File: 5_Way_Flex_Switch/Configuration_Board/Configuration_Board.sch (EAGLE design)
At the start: 1 part

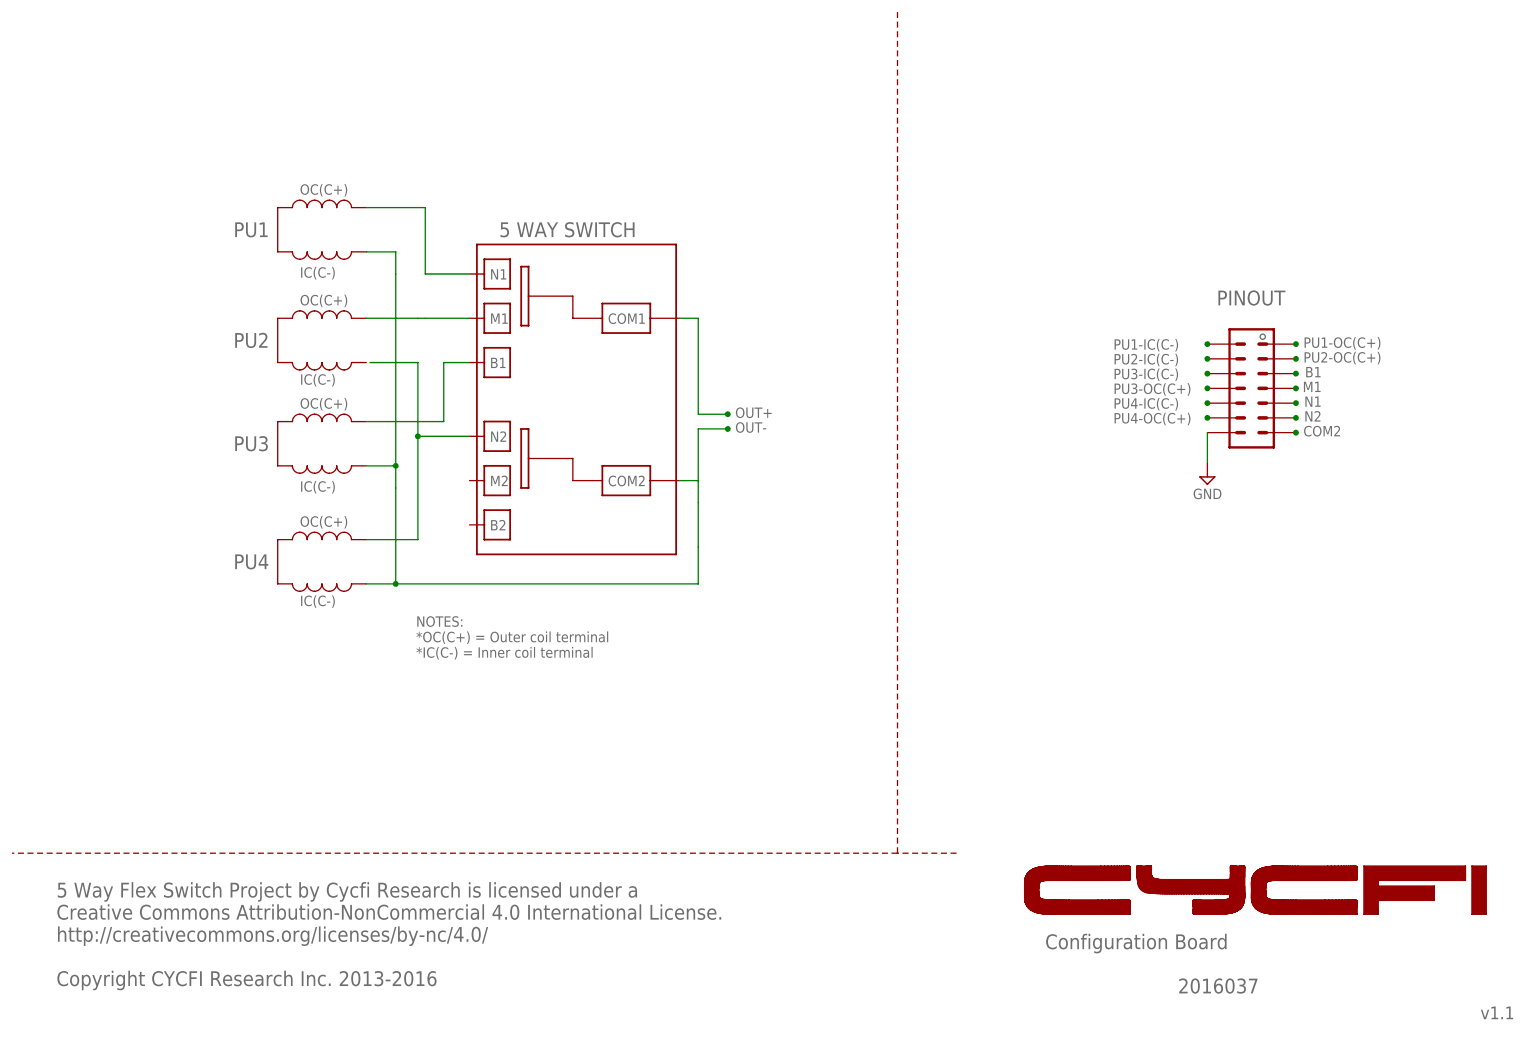
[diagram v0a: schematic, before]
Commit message: Updates/ label modifications to make them consistent
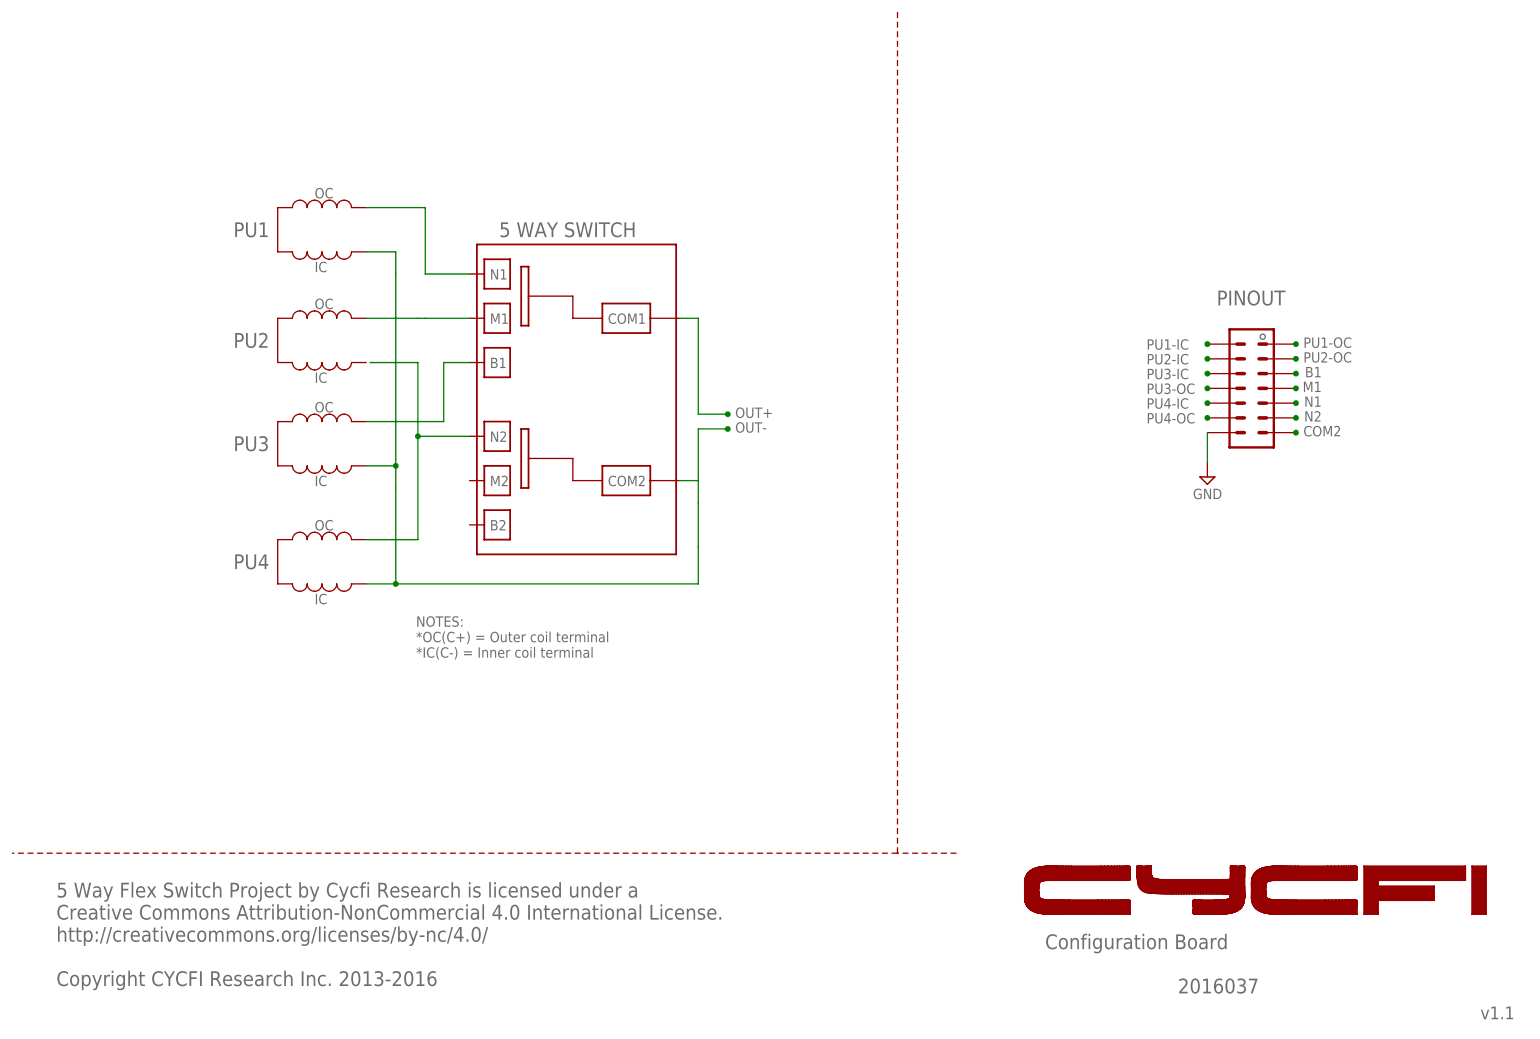
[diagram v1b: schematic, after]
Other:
- note added: "IC"
- note added: "OC"
- note added: "PU1-IC"
- note added: "PU1-OC"
- note added: "PU2-IC"
- note added: "PU2-OC"
- note added: "PU3-IC"
- note added: "PU3-OC"
- note added: "PU4-IC"
- note added: "PU4-OC"
- note removed: "IC(C-)"
- note removed: "OC(C+)"
- note removed: "PU1-IC(C-)"
- note removed: "PU1-OC(C+)"
- note removed: "PU2-IC(C-)"
- note removed: "PU2-OC(C+)"
- note removed: "PU3-IC(C-)"
- note removed: "PU3-OC(C+)"
- note removed: "PU4-IC(C-)"
- note removed: "PU4-OC(C+)"
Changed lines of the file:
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@@
 <setting verticaltext="up"/>
 </settings>
-<grid distance="0.1" unitdist="inch" unit="inch" style="lines" multiple="1" display="no" altdistance="0.01" altunitdist="inch" altunit="inch"/>
+<grid distance="0.1" unitdist="inch" unit="inch" style="lines" multiple="1" display="yes" altdistance="0.01" altunitdist="inch" altunit="inch"/>
 <layers>
 <layer number="1" name="Top" color="4" fill="1" visible="no" active="no"/>
@@
 <wire x1="58.42" y1="139.065" x2="60.96" y2="139.065" width="0.1524" layer="94"/>
 <wire x1="45.72" y1="146.685" x2="45.72" y2="139.065" width="0.1524" layer="94"/>
-<text x="49.53" y="134.62" size="1.778" layer="95">IC(C-)</text>
-<text x="49.53" y="148.9075" size="1.778" layer="95">OC(C+) </text>
 <wire x1="58.42" y1="127.635" x2="60.96" y2="127.635" width="0.1524" layer="94"/>
 <wire x1="58.42" y1="127.635" x2="57.15" y2="128.905" width="0.1524" layer="94" curve="90"/>
@@
 <vertex x="232.684540625" y="25.047221875"/>
 </polygon>
-<text x="49.53" y="129.8575" size="1.778" layer="95">OC(C+) </text>
-<text x="49.53" y="112.0775" size="1.778" layer="95">OC(C+) </text>
-<text x="49.53" y="91.7575" size="1.778" layer="95">OC(C+) </text>
-<text x="49.53" y="116.205" size="1.778" layer="95">IC(C-)</text>
-<text x="49.53" y="78.105" size="1.778" layer="95">IC(C-)</text>
-<text x="49.53" y="97.79" size="1.778" layer="95">IC(C-)</text>
 <text x="69.5325" y="69.215" size="1.778" layer="95">NOTES:
 *OC(C+) = Outer coil terminal
@@
 <text x="225.425" y="109.855" size="1.778" layer="95" rot="MR0">N2</text>
 <text x="207.3275" y="129.8575" size="2.54" layer="95">PINOUT</text>
-<text x="189.5475" y="122.2375" size="1.778" layer="95">PU1-IC(C-)</text>
-<text x="222.25" y="122.555" size="1.778" layer="95">PU1-OC(C+)</text>
-<text x="189.5475" y="119.6975" size="1.778" layer="95">PU2-IC(C-)</text>
-<text x="222.25" y="120.015" size="1.778" layer="95">PU2-OC(C+)</text>
-<text x="189.5475" y="117.1575" size="1.778" layer="95">PU3-IC(C-)</text>
-<text x="189.5475" y="114.6175" size="1.778" layer="95">PU3-OC(C+)</text>
-<text x="189.5475" y="112.0775" size="1.778" layer="95">PU4-IC(C-)</text>
-<text x="189.5475" y="109.5375" size="1.778" layer="95">PU4-OC(C+)</text>
+<text x="195.2625" y="122.2375" size="1.778" layer="95">PU1-IC</text>
+<text x="222.25" y="122.555" size="1.778" layer="95">PU1-OC</text>
+<text x="195.2625" y="119.6975" size="1.778" layer="95">PU2-IC</text>
+<text x="222.25" y="120.015" size="1.778" layer="95">PU2-OC</text>
+<text x="195.2625" y="117.1575" size="1.778" layer="95">PU3-IC</text>
+<text x="195.2625" y="114.6175" size="1.778" layer="95">PU3-OC</text>
+<text x="195.2625" y="112.0775" size="1.778" layer="95">PU4-IC</text>
+<text x="195.2625" y="109.5375" size="1.778" layer="95">PU4-OC</text>
 <text x="222.25" y="107.315" size="1.778" layer="95">COM2</text>
 <circle x="215.265" y="124.46" radius="0.4490125" width="0.1524" layer="95"/>
@@
 <wire x1="152.4" y1="35.56" x2="0" y2="35.56" width="0.1524" layer="94" style="longdash"/>
 <wire x1="152.4" y1="35.56" x2="152.4" y2="180.34" width="0.1524" layer="94" style="longdash"/>
+<text x="52.07" y="135.5725" size="1.778" layer="95">IC</text>
+<text x="52.07" y="148.2725" size="1.778" layer="95">OC</text>
+<text x="52.07" y="116.5225" size="1.778" layer="95">IC</text>
+<text x="52.07" y="129.2225" size="1.778" layer="95">OC</text>
+<text x="52.07" y="98.7425" size="1.778" layer="95">IC</text>
+<text x="52.07" y="111.4425" size="1.778" layer="95">OC</text>
+<text x="52.07" y="78.4225" size="1.778" layer="95">IC</text>
+<text x="52.07" y="91.1225" size="1.778" layer="95">OC</text>
 </plain>
 <instances>

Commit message: Licenses
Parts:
- removed U$1: CONFIGURATION_BRD_, CYCFI_Module_castellated:CONFIGURATION_BRD_
- added CB1: CONFIGURATION_BRD_CAST, CYCFI_Module_castellated:CONFIGURATION_BRD_CAST
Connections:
- removed net B1: U$1.3-OC, U$1.B
- removed net IN-: U$1.1-IC, U$1.3-IC, U$1.4-IC, U$1.IN-
- removed net M1: U$1.2-OC, U$1.M
- removed net N1: U$1.1-OC, U$1.N
- removed net N2: U$1.2-IC, U$1.4-OC, U$1.N2
- new net 1: CB1.3-OC, CB1.N1, CB1.OUT+
- new net 2: CB1.3-IC, CB1.4-OC, CB1.M1
- new net 3: CB1.1-OC, CB1.4-IC, CB1.B1, CB1.N2
- new net 4: CB1.COM1, CB1.COM2
- new net 5: CB1.1-IC, CB1.2-OC, CB1.M2
- new net 6: CB1.2-IC, CB1.B2, CB1.OUT-
- net GND: now also CB1.GND, CB1.GND1; no longer U$1.GND
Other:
- note added: "1-IC"
- note added: "1-OC"
- note added: "2-IC"
- note added: "2-OC"
- note added: "3-IC"
- note added: "3-OC"
- note added: "4-IC"
- note added: "4-OC"
- note added: "Configuration Board Project by Cycfi Research is licensed under a Creative Commons Attribution-NonCommercial 4.0 International License. http://creativecommons.org/licenses/by-nc/4.0/ Copyright CYCFI Research Inc. 2013-2016"
- note added: "GND"
- note added: "IC(C-)"
- note added: "OC(C+)"
- note removed: "5 Way Flex Switch Project by Cycfi Research is licensed under a Creative Commons Attribution-NonCommercial 4.0 International License. http://creativecommons.org/licenses/by-nc/4.0/ Copyright CYCFI Research Inc. 2013-2016"
- note removed: "IC"
- note removed: "OC"
- note removed: "PU1-IC"
- note removed: "PU1-OC"
- note removed: "PU2-IC"
- note removed: "PU2-OC"
- note removed: "PU3-IC"
- note removed: "PU3-OC"
- note removed: "PU4-IC"
- note removed: "PU4-OC"
